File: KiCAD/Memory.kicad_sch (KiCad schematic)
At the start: 6 parts

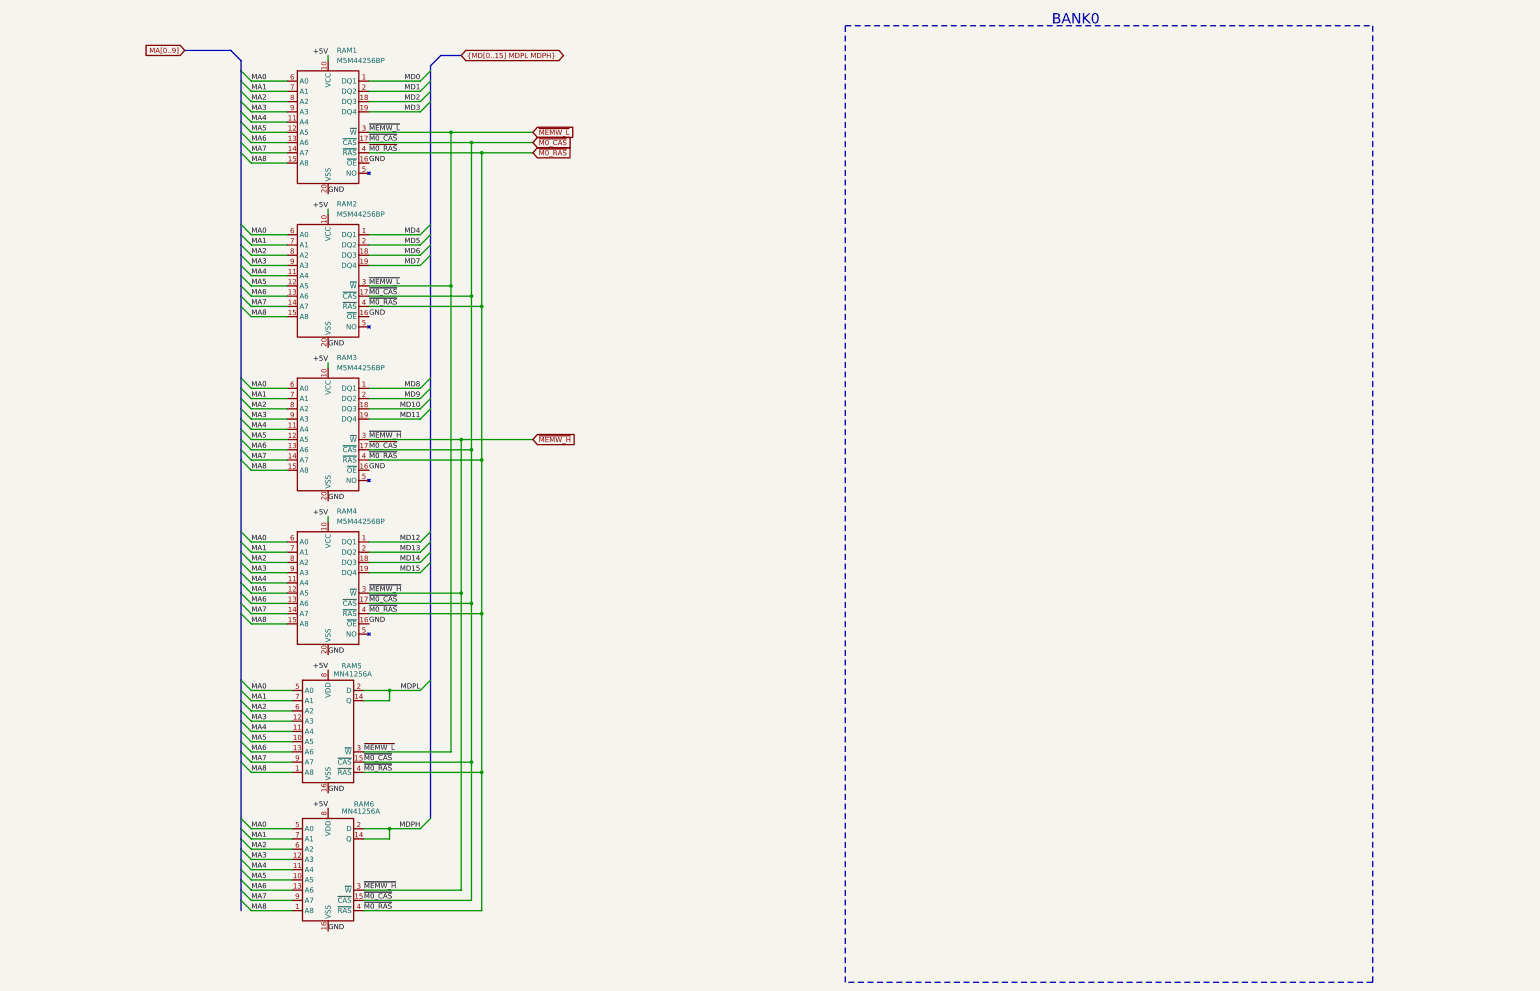
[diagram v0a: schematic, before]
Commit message: schematic update
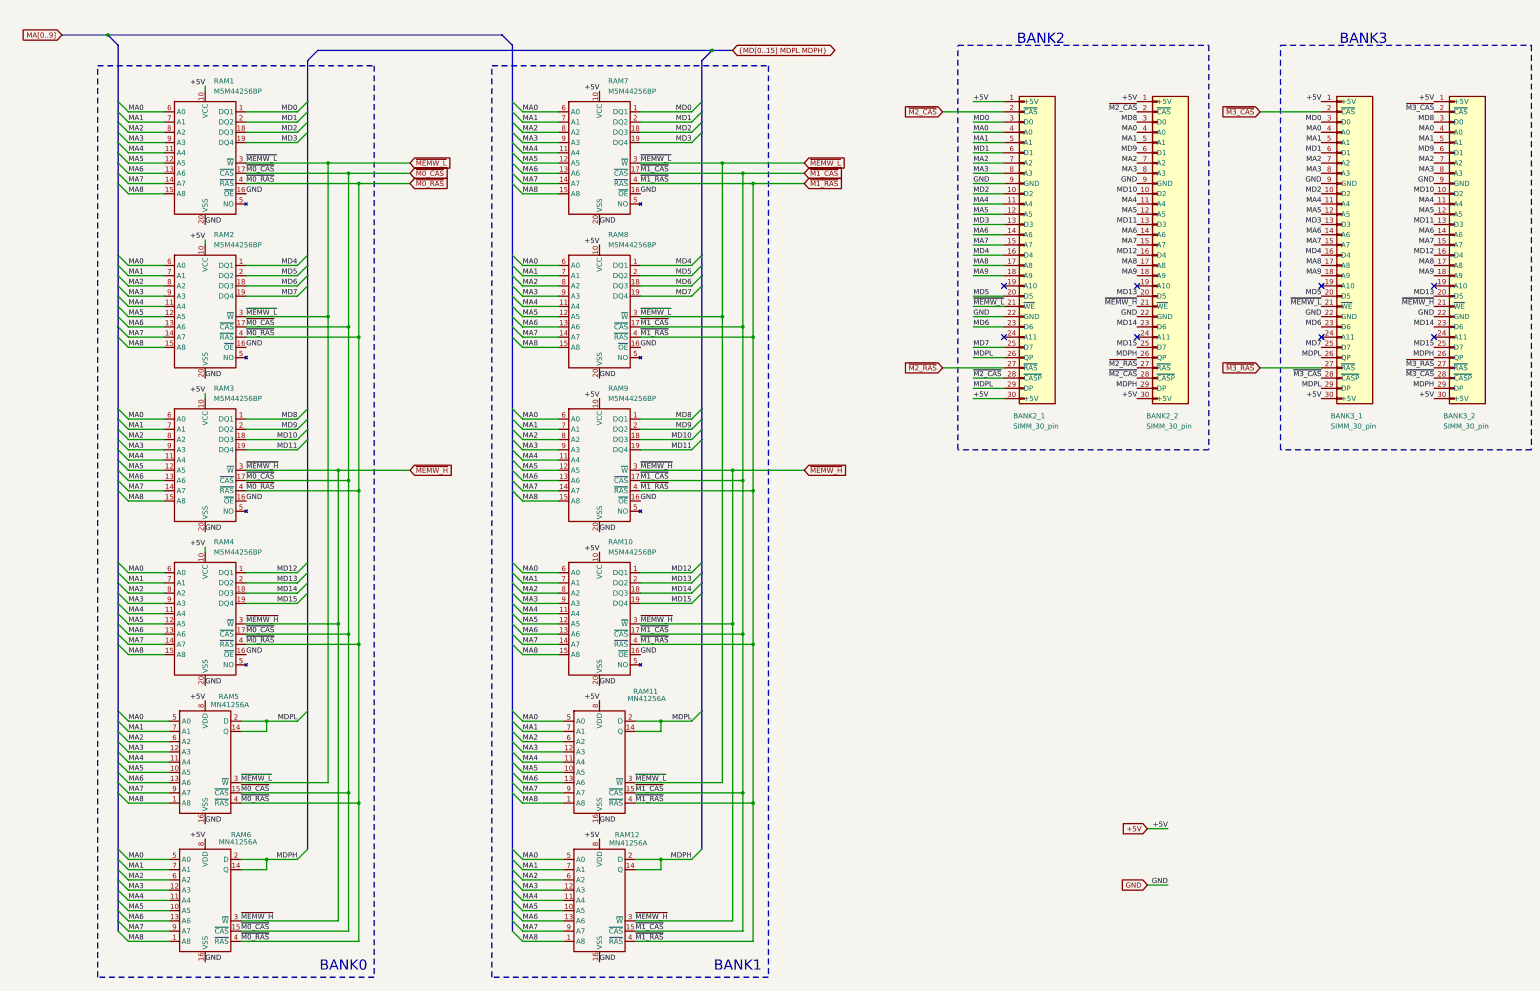
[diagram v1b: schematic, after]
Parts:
- added BANK2_1, BANK2_2, BANK3_1, BANK3_2: SIMM_30_pin, Connector_PinHeader_2.54mm:PinHeader_1x30_P2.54mm_Vertical, symbol _mine_d:SIMM_30_pin
- added RAM10, RAM7, RAM8, RAM9: M5M44256BP, Package_DIP:CERDIP-20_W7.62mm_SideBrazed, symbol _mine_d:44256
- added RAM11, RAM12: MN41256A, Package_DIP:CERDIP-16_W7.62mm_SideBrazed, symbol _mine_d:41256
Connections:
- net +5V: now also BANK2_1.1 (+5V), BANK2_1.30 (+5V), BANK2_2.1 (+5V), BANK2_2.30 (+5V), BANK3_1.1 (+5V), BANK3_1.30 (+5V), BANK3_2.1 (+5V), BANK3_2.30 (+5V), RAM10.10 (VCC), RAM11.8 (VDD), RAM12.8 (VDD), RAM7.10 (VCC), RAM8.10 (VCC), RAM9.10 (VCC)
- net GND: now also BANK2_1.22 (GND), BANK2_1.9 (GND), BANK2_2.22 (GND), BANK2_2.9 (GND), BANK3_1.22 (GND), BANK3_1.9 (GND), BANK3_2.22 (GND), BANK3_2.9 (GND), RAM10.16 (~{OE}), RAM10.20 (VSS), RAM11.16 (VSS), RAM12.16 (VSS), RAM7.16 (~{OE}), RAM7.20 (VSS), RAM8.16 (~{OE}), RAM8.20 (VSS), RAM9.16 (~{OE}), RAM9.20 (VSS)
- net MA0: now also BANK2_1.4 (A0), BANK2_2.4 (A0), BANK3_1.4 (A0), BANK3_2.4 (A0), RAM10.6 (A0), RAM11.5 (A0), RAM12.5 (A0), RAM7.6 (A0), RAM8.6 (A0), RAM9.6 (A0)
- net MA1: now also BANK2_1.5 (A1), BANK2_2.5 (A1), BANK3_1.5 (A1), BANK3_2.5 (A1), RAM10.7 (A1), RAM11.7 (A1), RAM12.7 (A1), RAM7.7 (A1), RAM8.7 (A1), RAM9.7 (A1)
- net MA2: now also BANK2_1.7 (A2), BANK2_2.7 (A2), BANK3_1.7 (A2), BANK3_2.7 (A2), RAM10.8 (A2), RAM11.6 (A2), RAM12.6 (A2), RAM7.8 (A2), RAM8.8 (A2), RAM9.8 (A2)
- net MA3: now also BANK2_1.8 (A3), BANK2_2.8 (A3), BANK3_1.8 (A3), BANK3_2.8 (A3), RAM10.9 (A3), RAM11.12 (A3), RAM12.12 (A3), RAM7.9 (A3), RAM8.9 (A3), RAM9.9 (A3)
- net MA4: now also BANK2_1.11 (A4), BANK2_2.11 (A4), BANK3_1.11 (A4), BANK3_2.11 (A4), RAM10.11 (A4), RAM11.11 (A4), RAM12.11 (A4), RAM7.11 (A4), RAM8.11 (A4), RAM9.11 (A4)
- net MA5: now also BANK2_1.12 (A5), BANK2_2.12 (A5), BANK3_1.12 (A5), BANK3_2.12 (A5), RAM10.12 (A5), RAM11.10 (A5), RAM12.10 (A5), RAM7.12 (A5), RAM8.12 (A5), RAM9.12 (A5)
- net MA6: now also BANK2_1.14 (A6), BANK2_2.14 (A6), BANK3_1.14 (A6), BANK3_2.14 (A6), RAM10.13 (A6), RAM11.13 (A6), RAM12.13 (A6), RAM7.13 (A6), RAM8.13 (A6), RAM9.13 (A6)
- net MA7: now also BANK2_1.15 (A7), BANK2_2.15 (A7), BANK3_1.15 (A7), BANK3_2.15 (A7), RAM10.14 (A7), RAM11.9 (A7), RAM12.9 (A7), RAM7.14 (A7), RAM8.14 (A7), RAM9.14 (A7)
- net MA8: now also BANK2_1.17 (A8), BANK2_2.17 (A8), BANK3_1.17 (A8), BANK3_2.17 (A8), RAM10.15 (A8), RAM11.1 (A8), RAM12.1 (A8), RAM7.15 (A8), RAM8.15 (A8), RAM9.15 (A8)
- net MD0: now also BANK2_1.3 (D0), BANK3_1.3 (D0), RAM7.1 (DQ1)
- net MD1: now also BANK2_1.6 (D1), BANK3_1.6 (D1), RAM7.2 (DQ2)
- net MD10: now also BANK2_2.10 (D2), BANK3_2.10 (D2), RAM9.18 (DQ3)
- net MD11: now also BANK2_2.13 (D3), BANK3_2.13 (D3), RAM9.19 (DQ4)
- net MD12: now also BANK2_2.16 (D4), BANK3_2.16 (D4), RAM10.1 (DQ1)
- net MD13: now also BANK2_2.20 (D5), BANK3_2.20 (D5), RAM10.2 (DQ2)
- net MD14: now also BANK2_2.23 (D6), BANK3_2.23 (D6), RAM10.18 (DQ3)
- net MD15: now also BANK2_2.25 (D7), BANK3_2.25 (D7), RAM10.19 (DQ4)
- net MD2: now also BANK2_1.10 (D2), BANK3_1.10 (D2), RAM7.18 (DQ3)
- net MD3: now also BANK2_1.13 (D3), BANK3_1.13 (D3), RAM7.19 (DQ4)
- net MD4: now also BANK2_1.16 (D4), BANK3_1.16 (D4), RAM8.1 (DQ1)
- net MD5: now also BANK2_1.20 (D5), BANK3_1.20 (D5), RAM8.2 (DQ2)
- net MD6: now also BANK2_1.23 (D6), BANK3_1.23 (D6), RAM8.18 (DQ3)
- net MD7: now also BANK2_1.25 (D7), BANK3_1.25 (D7), RAM8.19 (DQ4)
- net MD8: now also BANK2_2.3 (D0), BANK3_2.3 (D0), RAM9.1 (DQ1)
- net MD9: now also BANK2_2.6 (D1), BANK3_2.6 (D1), RAM9.2 (DQ2)
- net MDPH: now also BANK2_2.26 (QP), BANK2_2.29 (DP), BANK3_2.26 (QP), BANK3_2.29 (DP), RAM12.14 (Q), RAM12.2 (D)
- net MDPL: now also BANK2_1.26 (QP), BANK2_1.29 (DP), BANK3_1.26 (QP), BANK3_1.29 (DP), RAM11.14 (Q), RAM11.2 (D)
- net ~{MEMW_H}: now also BANK2_2.21 (~{WE}), BANK3_2.21 (~{WE}), RAM10.3 (~{W}), RAM12.3 (~{W}), RAM9.3 (~{W})
- net ~{MEMW_L}: now also BANK2_1.21 (~{WE}), BANK3_1.21 (~{WE}), RAM11.3 (~{W}), RAM7.3 (~{W}), RAM8.3 (~{W})
- new net MA9: BANK2_1.18 (A9), BANK2_2.18 (A9), BANK3_1.18 (A9), BANK3_2.18 (A9)
- new net ~{M1_CAS}: RAM10.17 (~{CAS}), RAM11.15 (~{CAS}), RAM12.15 (~{CAS}), RAM7.17 (~{CAS}), RAM8.17 (~{CAS}), RAM9.17 (~{CAS})
- new net ~{M1_RAS}: RAM10.4 (~{RAS}), RAM11.4 (~{RAS}), RAM12.4 (~{RAS}), RAM7.4 (~{RAS}), RAM8.4 (~{RAS}), RAM9.4 (~{RAS})
- new net ~{M2_CAS}: BANK2_1.2 (~{CAS}), BANK2_1.28 (~{CASP}), BANK2_2.2 (~{CAS}), BANK2_2.28 (~{CASP})
- new net ~{M2_RAS}: BANK2_1.27 (~{RAS}), BANK2_2.27 (~{RAS})
- new net ~{M3_CAS}: BANK3_1.2 (~{CAS}), BANK3_1.28 (~{CASP}), BANK3_2.2 (~{CAS}), BANK3_2.28 (~{CASP})
- new net ~{M3_RAS}: BANK3_1.27 (~{RAS}), BANK3_2.27 (~{RAS})
- no-connect marks 0 -> 8
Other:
- note added: "BANK1"
- note added: "BANK2"
- note added: "BANK3"
- moved on the sheet: RAM1, RAM2, RAM3, RAM4, RAM5, RAM6

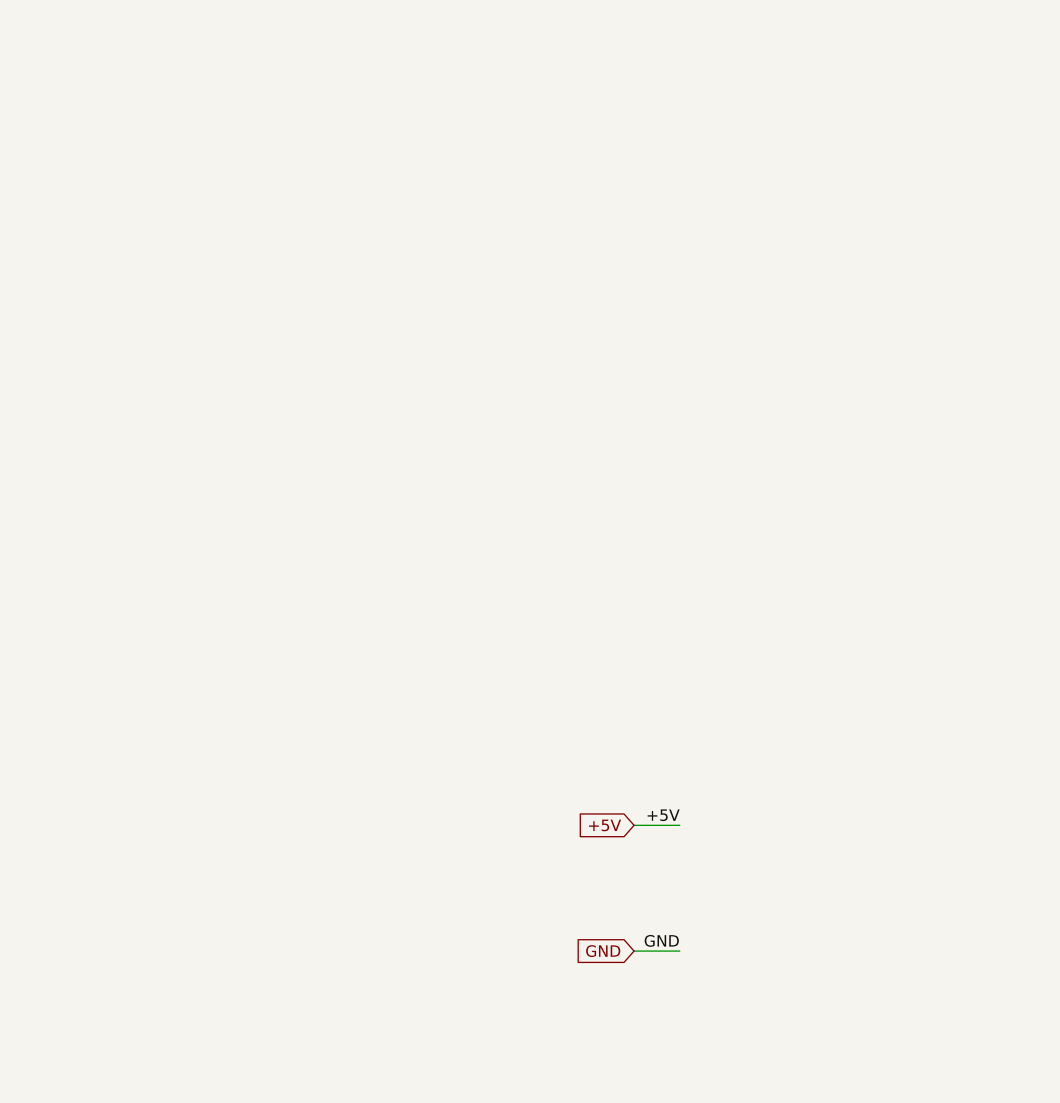
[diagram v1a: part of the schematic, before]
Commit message: schematics update
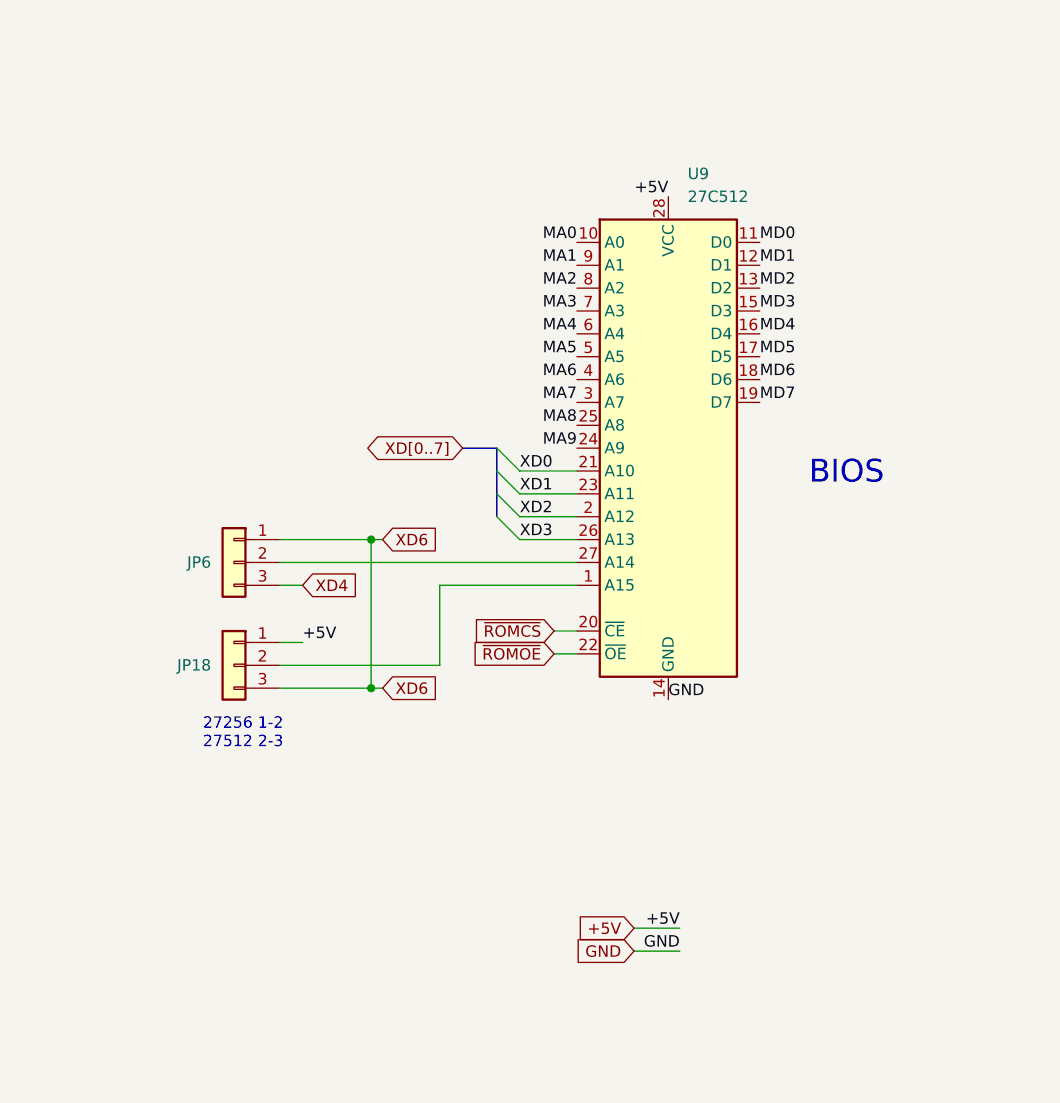
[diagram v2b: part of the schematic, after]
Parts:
- added JP18, JP6: Conn_01x03, Connector_PinHeader_2.54mm:PinHeader_1x03_P2.54mm_Vertical, symbol Connector_Generic:Conn_01x03
- added U9: 27C512, Package_DIP:DIP-28_W15.24mm, symbol Memory_EPROM:27C512
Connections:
- net +5V: now also JP18.1 (Pin_1), U9.28 (VCC)
- net GND: now also U9.14 (GND)
- net MA0: now also U9.10 (A0)
- net MA1: now also U9.9 (A1)
- net MA2: now also U9.8 (A2)
- net MA3: now also U9.7 (A3)
- net MA4: now also U9.6 (A4)
- net MA5: now also U9.5 (A5)
- net MA6: now also U9.4 (A6)
- net MA7: now also U9.3 (A7)
- net MA8: now also U9.25 (A8)
- net MA9: now also U9.24 (A9)
- net MD0: now also U9.11 (D0)
- net MD1: now also U9.12 (D1)
- net MD2: now also U9.13 (D2)
- net MD3: now also U9.15 (D3)
- net MD4: now also U9.16 (D4)
- net MD5: now also U9.17 (D5)
- net MD6: now also U9.18 (D6)
- net MD7: now also U9.19 (D7)
- new net: JP18.2 (Pin_2), U9.1 (A15)
- new net: JP6.2 (Pin_2), U9.27 (A14)
- new net XD0: U9.21 (A10)
- new net XD1: U9.23 (A11)
- new net XD2: U9.2 (A12)
- new net XD3: U9.26 (A13)
- new net XD4: JP6.3 (Pin_3)
- new net XD6: JP18.3 (Pin_3), JP6.1 (Pin_1)
- new net ~{ROMCS}: U9.20 (~{CE})
- new net ~{ROMOE}: U9.22 (~{OE})
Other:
- note added: "27256 1-2 27512 2-3"
- note added: "BIOS"
- title: (none) -> PC/AT 286
